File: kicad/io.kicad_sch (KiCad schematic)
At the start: 22 parts, among them J7 Conn_01x10_Pin, J9 Conn_01x10_Pin, U12 74LS574, U4 74LS574, U5 74HC245

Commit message: pcb: fix value of RN1
also accidentally pushed release2 data
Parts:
- RN1: value R_Network08 -> 4K7
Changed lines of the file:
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@@
 		(fields_autoplaced yes)
 		(property "Reference" "RN1"
-			(at 139.7 110.7439 0)
+			(at 139.192 110.8018 0)
 			(effects
 				(font
@@
 			)
 		)
-		(property "Value" "R_Network08"
-			(at 139.7 113.2839 0)
+		(property "Value" "4K7"
+			(at 139.192 113.2261 0)
 			(effects
 				(font

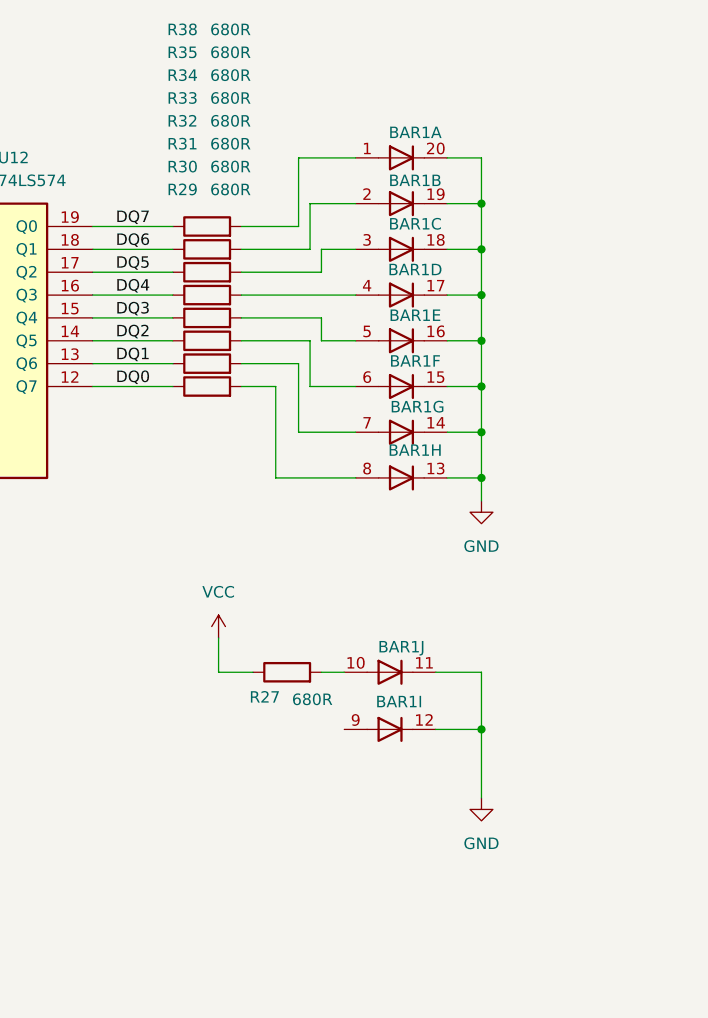
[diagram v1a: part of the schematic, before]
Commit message: update to kicad10, v1_r3 release
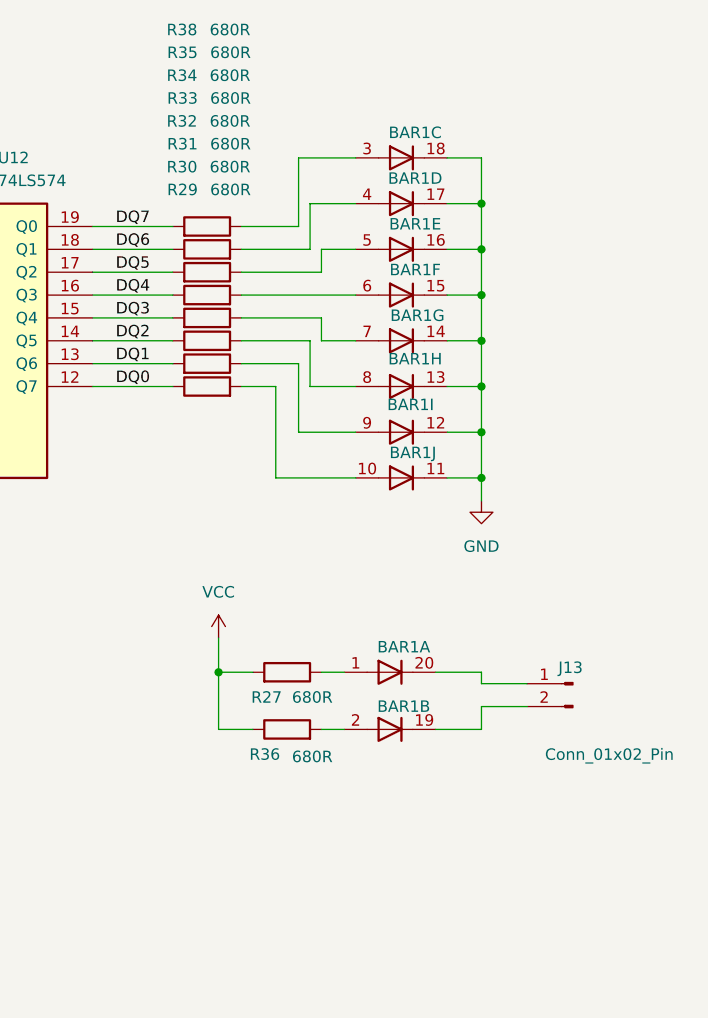
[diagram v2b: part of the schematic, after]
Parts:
- added J13: Conn_01x02_Pin, Connector_PinHeader_2.54mm:PinHeader_1x02_P2.54mm_Vertical, symbol Connector:Conn_01x02_Pin
- added R36: 680R, Resistor_THT:R_Axial_DIN0207_L6.3mm_D2.5mm_P2.54mm_Vertical, symbol Device:R
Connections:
- net DQ1: now also R30.2; no longer R30.1
- net DQ3: now also R32.2; no longer R32.1
- net DQ5: now also R34.2; no longer R34.1
- net DQ7: now also R38.2; no longer R38.1
- net GND: no longer BAR1.19 (K), BAR1.20 (K)
- net VCC: now also R27.2, R36.1; no longer R27.1
- net at BAR1.10 (A): now also R29.2; no longer R27.2
- net at BAR1.9 (A): now also R30.1
- net at BAR1.2 (A): now also R36.2; no longer R35.2
- net at BAR1.8 (A): now also R31.2; no longer R29.2
- net at BAR1.1 (A): now also R27.1; no longer R38.2
- net at BAR1.6 (A): now also R33.2; no longer R31.2
- net at BAR1.5 (A): now also R34.1; no longer R32.2
- net at BAR1.3 (A): now also R38.1; no longer R34.2
- net at BAR1.4 (A): now also R35.2; no longer R33.2
- net at BAR1.7 (A): now also R32.1; no longer R30.2
- new net: BAR1.19 (K), J13.2 (Pin_2)
- new net: BAR1.20 (K), J13.1 (Pin_1)
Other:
- moved on the sheet: BAR1A, BAR1B, BAR1C, BAR1D, BAR1E, BAR1F, BAR1G, BAR1H, BAR1I, BAR1J, R27, R30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

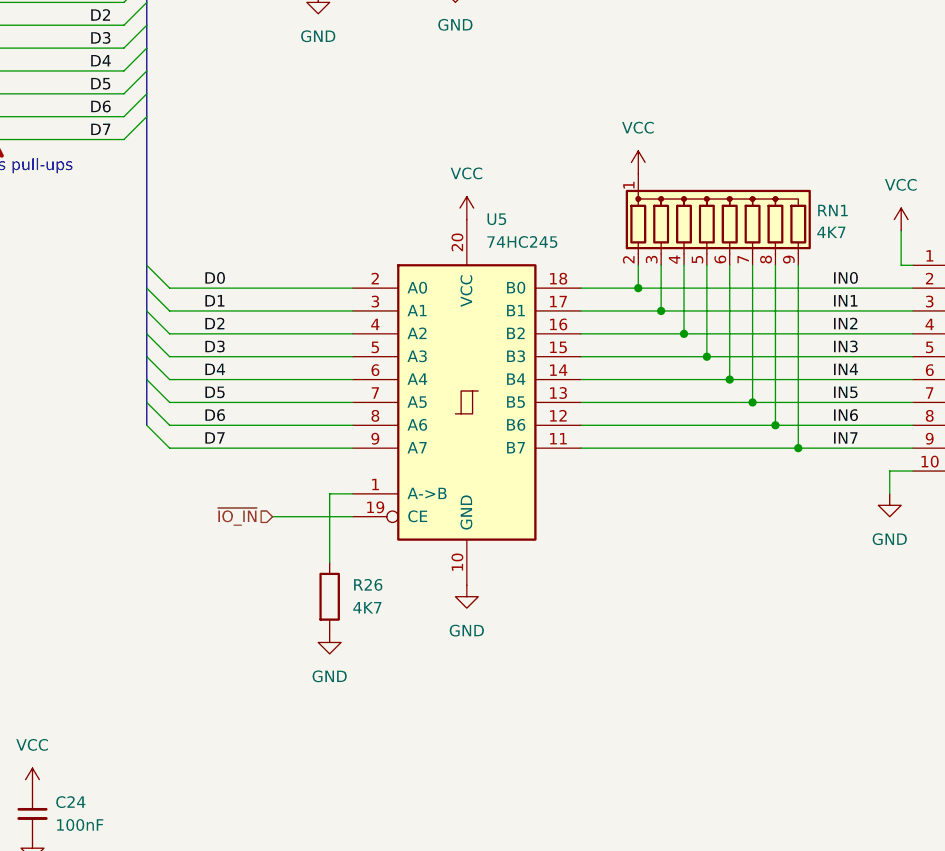
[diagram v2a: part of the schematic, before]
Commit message: updated to use 74x574 for input, then drc fixes
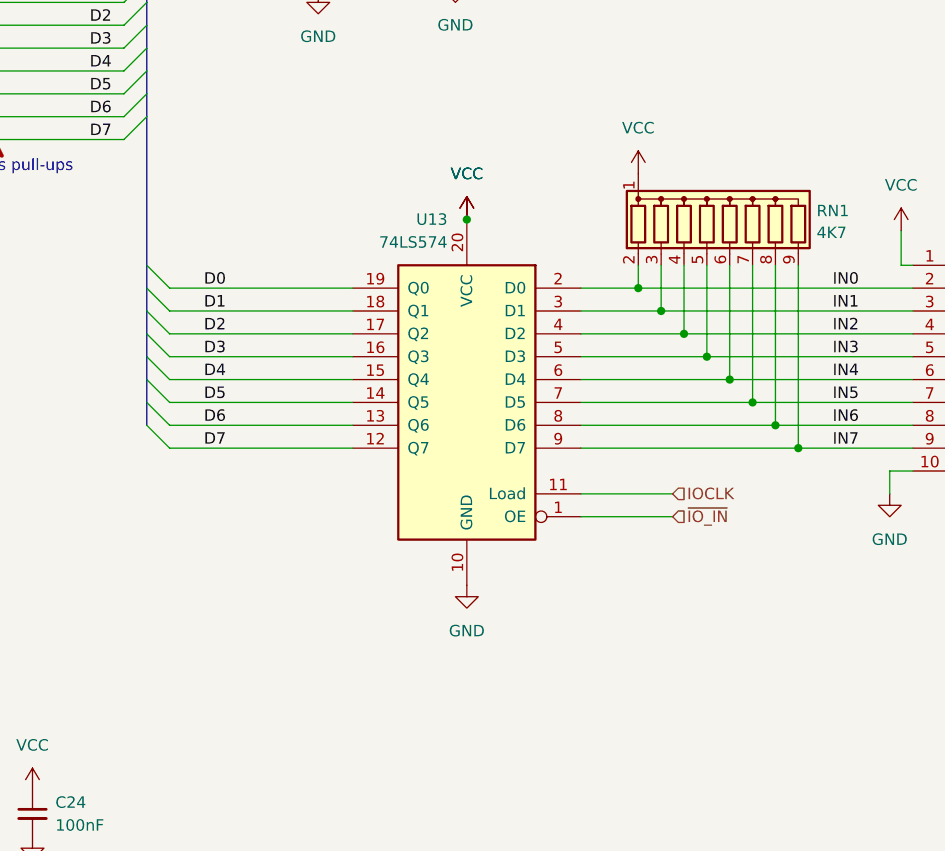
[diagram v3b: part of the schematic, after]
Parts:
- removed R26: 4K7, Resistor_THT:R_Axial_DIN0207_L6.3mm_D2.5mm_P10.16mm_Horizontal, symbol Device:R
- removed U5: 74HC245, Package_DIP:DIP-20_W7.62mm, symbol 74xx:74HC245
- added U13: 74LS574, Package_DIP:DIP-20_W7.62mm, symbol 74xx:74LS573
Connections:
- net D0: now also U13.19 (Q0)
- net D1: now also U13.18 (Q1)
- net D2: now also U13.17 (Q2)
- net D3: now also U13.16 (Q3)
- net D4: now also U13.15 (Q4)
- net D5: now also U13.14 (Q5)
- net D6: now also U13.13 (Q6)
- net D7: now also U13.12 (Q7)
- net GND: now also U13.10 (GND)
- net IN0: now also U13.2 (D0)
- net IN1: now also U13.3 (D1)
- net IN2: now also U13.4 (D2)
- net IN3: now also U13.5 (D3)
- net IN4: now also U13.6 (D4)
- net IN5: now also U13.7 (D5)
- net IN6: now also U13.8 (D6)
- net IN7: now also U13.9 (D7)
- net VCC: now also U13.20 (VCC)
- net ~{IO_IN}: now also U13.1 (OE)
- new net IOCLK: U13.11 (Load)
